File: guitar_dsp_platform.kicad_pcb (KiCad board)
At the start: 4 copper layers, 122 x 122 mm, 159 parts, among them J201 NMJ6HCD2, J202 NMJ6HCD2, J203 NMJ6HCD2, J204 NMJ6HCD2, J401 57PC5F, J402 57PC5F, J403 I2S, J501 PJ-002AH-SMT-TR, Q401 MMBT3904, Q501 SI2371EDS-T1-GE3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

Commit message: Minor layout tweaks
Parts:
- moved C401 2.25 mm to (143.5, 132.0)
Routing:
- net Net-(C401-Pad1): track 6.21 -> 3.96 mm
- net GND: track 145.2 -> 147.0 mm
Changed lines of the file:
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@@
       (net 92 "GND") (pinfunction "Pin_3") (pintype "passive"))
     (pad "4" thru_hole oval locked (at 2.54 2.54 270) (size 1.7 1.7) (drill 1) (layers *.Cu *.Mask)
-      (net 109 "/ESP32/LRCK") (pinfunction "Pin_4") (pintype "passive") (clearance 0.2))
+      (net 109 "/ESP32/LRCK") (pinfunction "Pin_4") (pintype "passive"))
     (pad "5" thru_hole oval locked (at 0 5.08 270) (size 1.7 1.7) (drill 1) (layers *.Cu *.Mask)
       (net 92 "GND") (pinfunction "Pin_5") (pintype "passive"))
     (pad "6" thru_hole oval locked (at 2.54 5.08 270) (size 1.7 1.7) (drill 1) (layers *.Cu *.Mask)
-      (net 110 "/ESP32/BCK") (pinfunction "Pin_6") (pintype "passive") (clearance 0.2))
+      (net 110 "/ESP32/BCK") (pinfunction "Pin_6") (pintype "passive"))
     (pad "7" thru_hole oval locked (at 0 7.62 270) (size 1.7 1.7) (drill 1) (layers *.Cu *.Mask)
       (net 92 "GND") (pinfunction "Pin_7") (pintype "passive"))
     (pad "8" thru_hole oval locked (at 2.54 7.62 270) (size 1.7 1.7) (drill 1) (layers *.Cu *.Mask)
-      (net 111 "/ESP32/SCK") (pinfunction "Pin_8") (pintype "passive") (clearance 0.2))
+      (net 111 "/ESP32/SCK") (pinfunction "Pin_8") (pintype "passive"))
     (pad "9" thru_hole oval locked (at 0 10.16 270) (size 1.7 1.7) (drill 1) (layers *.Cu *.Mask)
       (net 92 "GND") (pinfunction "Pin_9") (pintype "passive"))
@@
   )
   (footprint "Capacitor_SMD:C_0805_2012Metric_Pad1.18x1.45mm_HandSolder" (layer "F.Cu")
-    (at 141.25 132 180)
+    (at 143.5 132 180)
     (descr "Capacitor SMD 0805 (2012 Metric), square (rectangular) end terminal, IPC_7351 nominal with elongated pad for handsoldering. (Body size source: IPC-SM-782 page 76, https://www.pcb-3d.com/wordpress/wp-content/uploads/ipc-sm-782a_amendment_1_and_2.pdf, https://docs.google.com/spreadsheets/d/1BsfQQcO9C6DZCsRaXUlFlo91Tg2WpOkGARC1WS5S8t0/edit?usp=sharing), generated with kicad-footprint-generator")
     (tags "capacitor handsolder")
@@
     (property "Sheetname" "ESP32")
     (attr smd)
-    (fp_text reference "C401" (at 0 -1.68) (layer "F.SilkS")
+    (fp_text reference "C401" (at 0 -2.5) (layer "F.SilkS")
       (effects (font (size 1 1) (thickness 0.15)))
     )
@@
   (segment (start 66.135 95.115) (end 58.75 95.115) (width 0.4) (layer "F.Cu") (net 42))
   (segment (start 70.25 91) (end 66.135 95.115) (width 0.4) (layer "F.Cu") (net 42))
-  (segment (start 142.2875 132) (end 148.5 132) (width 0.4) (layer "F.Cu") (net 43))
+  (segment (start 144.5375 132) (end 148.5 132) (width 1) (layer "F.Cu") (net 43))
   (segment (start 65.516 47.736) (end 64.262 47.736) (width 0.4) (layer "F.Cu") (net 44))
   (segment (start 124 85) (end 124.75 85) (width 0.25) (layer "F.Cu") (net 44))
@@
   (via (at 60.25 47) (size 0.6) (drill 0.3) (layers "F.Cu" "B.Cu") (free) (net 92))
   (via (at 76.25 108.75) (size 0.6) (drill 0.3) (layers "F.Cu" "B.Cu") (free) (net 92))
-  (via (at 140.25 130.5) (size 0.6) (drill 0.3) (layers "F.Cu" "B.Cu") (free) (net 92))
+  (via (at 142.5 130.5) (size 0.6) (drill 0.3) (layers "F.Cu" "B.Cu") (free) (net 92))
   (via (at 85.25 58.75) (size 0.6) (drill 0.3) (layers "F.Cu" "B.Cu") (net 92))
   (via (at 78.25 105.75) (size 0.6) (drill 0.3) (layers "F.Cu" "B.Cu") (net 92))
@@
   (via (at 107.204 96.204) (size 0.6) (drill 0.3) (layers "F.Cu" "B.Cu") (net 92))
   (via (at 118 157) (size 0.6) (drill 0.3) (layers "F.Cu" "B.Cu") (net 92))
-  (via (at 138.75 132) (size 0.6) (drill 0.3) (layers "F.Cu" "B.Cu") (free) (net 92))
+  (via (at 141 132) (size 0.6) (drill 0.3) (layers "F.Cu" "B.Cu") (free) (net 92))
   (via (at 124.75 62) (size 0.6) (drill 0.3) (layers "F.Cu" "B.Cu") (free) (net 92))
   (via (at 113 62) (size 0.6) (drill 0.3) (layers "F.Cu" "B.Cu") (free) (net 92))
@@
   (via (at 127.5 156.75) (size 0.6) (drill 0.3) (layers "F.Cu" "B.Cu") (net 92))
   (via (at 125.333333 40) (size 0.6) (drill 0.3) (layers "F.Cu" "B.Cu") (net 92))
-  (via (at 140.25 133.5) (size 0.6) (drill 0.3) (layers "F.Cu" "B.Cu") (free) (net 92))
+  (via (at 142.5 133.5) (size 0.6) (drill 0.3) (layers "F.Cu" "B.Cu") (free) (net 92))
   (via (at 145 150.25) (size 0.6) (drill 0.3) (layers "F.Cu" "B.Cu") (free) (net 92))
   (via (at 115.75 141.25) (size 0.6) (drill 0.3) (layers "F.Cu" "B.Cu") (free) (net 92))
@@
   (segment (start 121.42 95.46) (end 122.669511 96.709511) (width 0.4) (layer "In2.Cu") (net 92))
   (segment (start 129.04 95.46) (end 127.790489 96.709511) (width 0.4) (layer "In2.Cu") (net 92))
+  (segment (start 127.749511 96.709511) (end 127.790489 96.709511) (width 0.4) (layer "In2.Cu") (net 92))
   (segment (start 130.5 96.92) (end 129.04 95.46) (width 0.4) (layer "In2.Cu") (net 92))
   (segment (start 122.000489 99.249511) (end 120.749511 99.249511) (width 0.4) (layer "In2.Cu") (net 92))
   (segment (start 117.630489 98.517565) (end 118.612924 99.5) (width 0.4) (layer "In2.Cu") (net 92))
+  (segment (start 126.5 95.46) (end 127.749511 96.709511) (width 0.4) (layer "In2.Cu") (net 92))
   (segment (start 127.790489 96.709511) (end 127.790489 98.476587) (width 0.4) (layer "In2.Cu") (net 92))
   (segment (start 120.749511 99.249511) (end 120.129511 98.629511) (width 0.4) (layer "In2.Cu") (net 92))

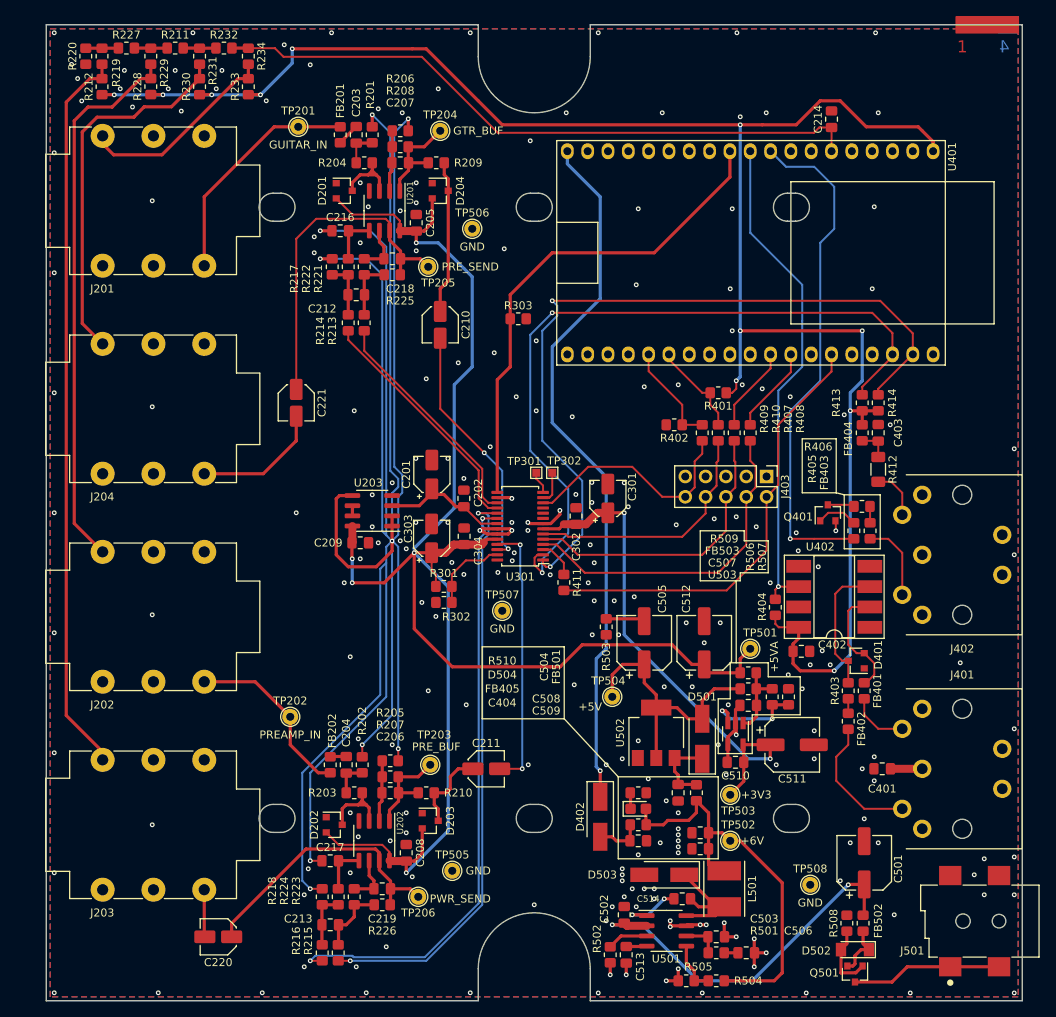
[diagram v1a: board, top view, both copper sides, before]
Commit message: Tweak mechanical design
1/4 inch jacks are now flush with the faceplate. Reduced the gap between
MIDI jack and back faceplate.
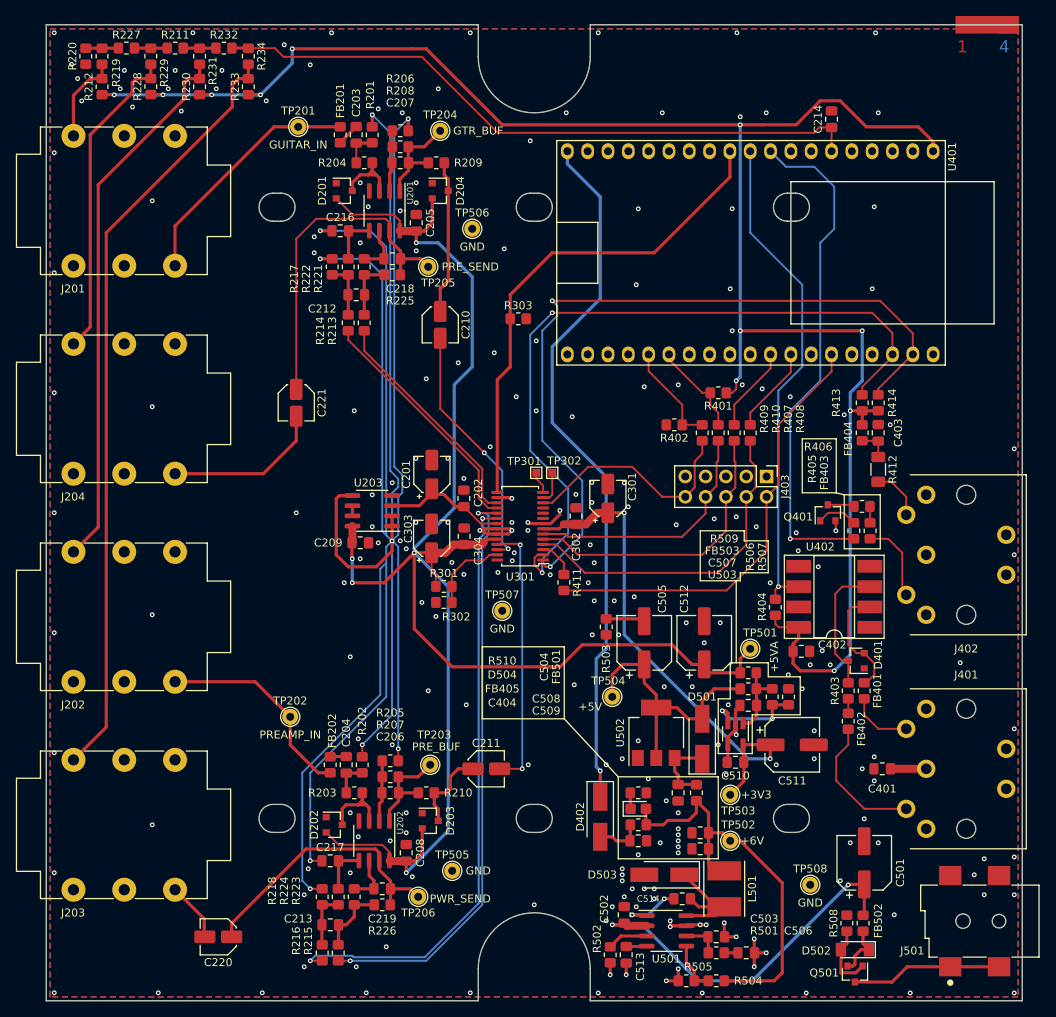
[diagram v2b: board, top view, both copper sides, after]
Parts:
- C501, C505, C511, C512: footprint Capacitor_SMD:CP_Elec_6.3x5.8 -> Capacitor_SMD:CP_Elec_6.3x7.7
- Q501: value SI2371EDS-T1-GE3 -> SI2369DS-T1-BE3
- moved J201 3.65 mm to (38.4, 61.0)
- moved J202 3.65 mm to (38.4, 113.0)
- moved J203 3.65 mm to (38.4, 139.0)
- moved J204 3.65 mm to (38.4, 87.0)
- moved J401 0.50 mm to (154.0, 132.0)
- moved J402 0.50 mm to (154.0, 105.2)
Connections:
- R212 pad 2: /Analogue/AMP_DET_JACK -> /Analogue/G_DET_JACK
- R219 pad 2: /Analogue/AMP_DET_JACK -> /Analogue/G_DET_JACK
- R228 pad 2: /Analogue/PRE_I_DET_JACK -> /Analogue/PRE_O_DET_JACK
- R229 pad 2: /Analogue/PRE_I_DET_JACK -> /Analogue/PRE_O_DET_JACK
- R230 pad 2: /Analogue/PRE_O_DET_JACK -> /Analogue/PRE_I_DET_JACK
- R231 pad 2: /Analogue/PRE_O_DET_JACK -> /Analogue/PRE_I_DET_JACK
- R233 pad 2: /Analogue/G_DET_JACK -> /Analogue/AMP_DET_JACK
- R234 pad 2: /Analogue/G_DET_JACK -> /Analogue/AMP_DET_JACK
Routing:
- net /Analogue/G_DET_JACK: track 24.5 -> 11.3 mm
- net /Analogue/PRE_O_DET_JACK: track 46.8 -> 40.0 mm
- net /Analogue/AMP_DET_JACK: track 90.6 -> 96.7 mm
- net Net-(FB202-Pad2): track 22.5 -> 26.2 mm
- net Net-(C221-Pad2): track 16.3 -> 19.9 mm
- net Net-(C220-Pad2): track 5.92 -> 7.43 mm
- net Net-(FB201-Pad2): track 29.2 -> 30.8 mm
- net /Analogue/PRE_I_DET_JACK: track 68.9 -> 68.3 mm
- net Net-(FB402-Pad2): track 16.8 -> 17.3 mm
- net Net-(FB401-Pad2): track 7.47 -> 7.97 mm
- net Net-(C401-Pad1): track 3.96 -> 4.46 mm
